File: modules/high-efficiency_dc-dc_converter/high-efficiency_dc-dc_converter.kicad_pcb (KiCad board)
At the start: 2 copper layers, 27.9 x 20.3 mm, 13 parts

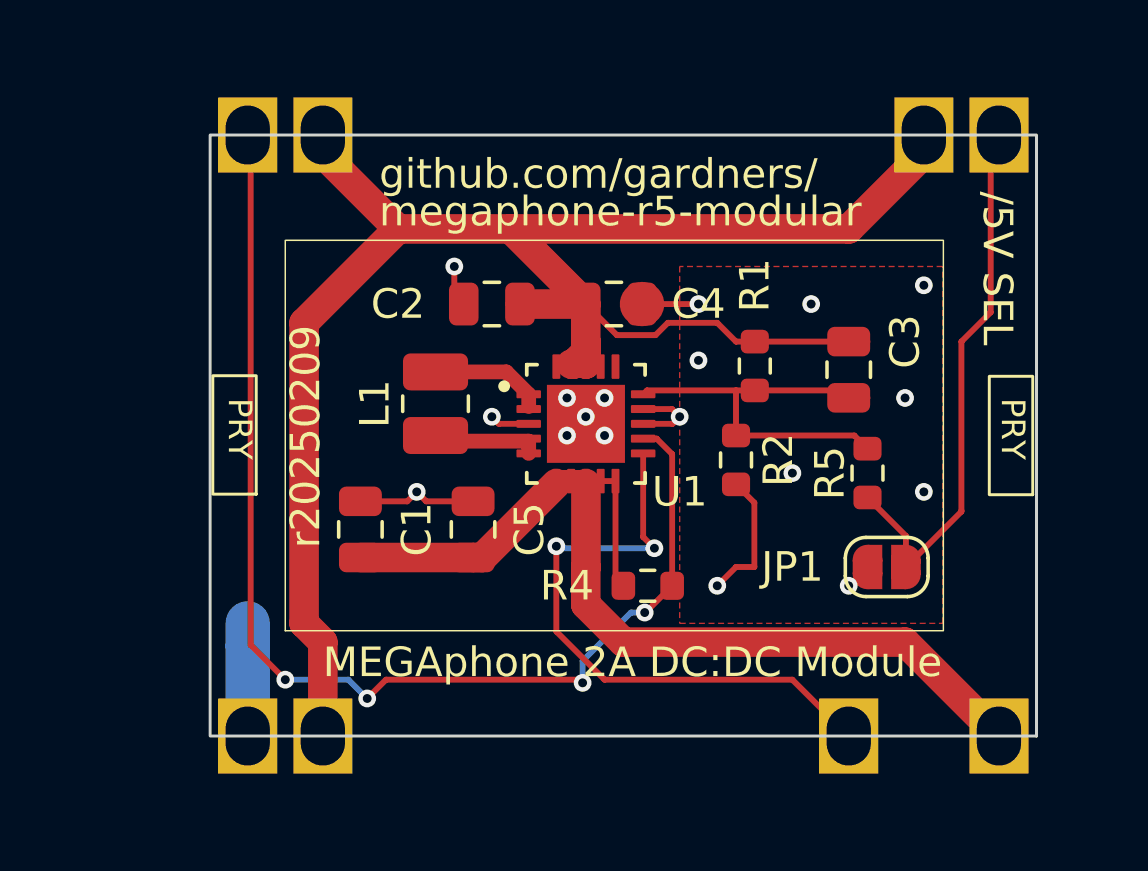
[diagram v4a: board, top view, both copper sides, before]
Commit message: update dc-dc converter footprint
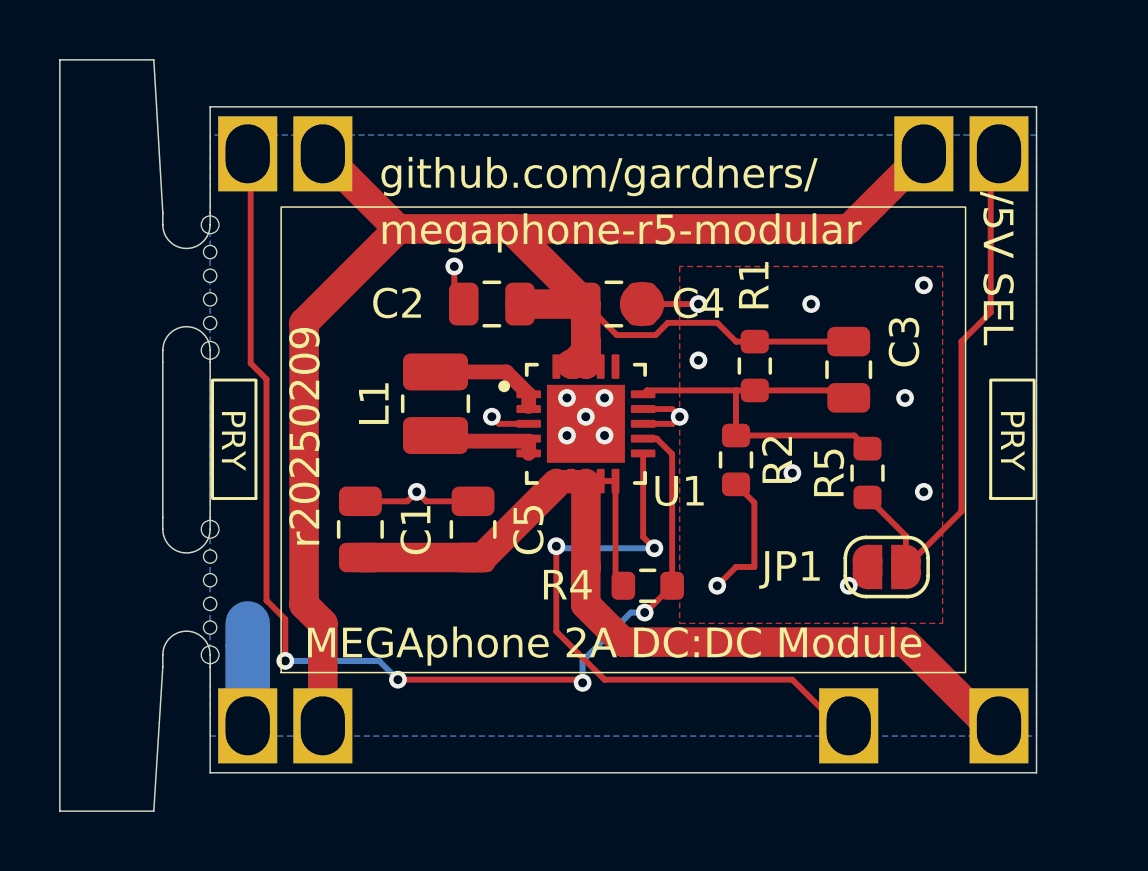
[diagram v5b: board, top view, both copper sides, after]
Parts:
- M1: footprint MegaCastle:MegaCastle2x11Wide-Module-I13.2x22.25-KA0780C -> MegaCastle:MegaCastle2x11-Module-I15.7x23.1-MA0780C-PANEL-NIBBLE
- moved M1 1.28 mm to (63.5, 40.8)
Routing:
- net MODE: track 40.2 -> 39.3 mm
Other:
- board size 27.9 x 20.3 mm -> 29.5 x 22.5 mm
- board text added: "r20250222"
